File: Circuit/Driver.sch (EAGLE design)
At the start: 1 part

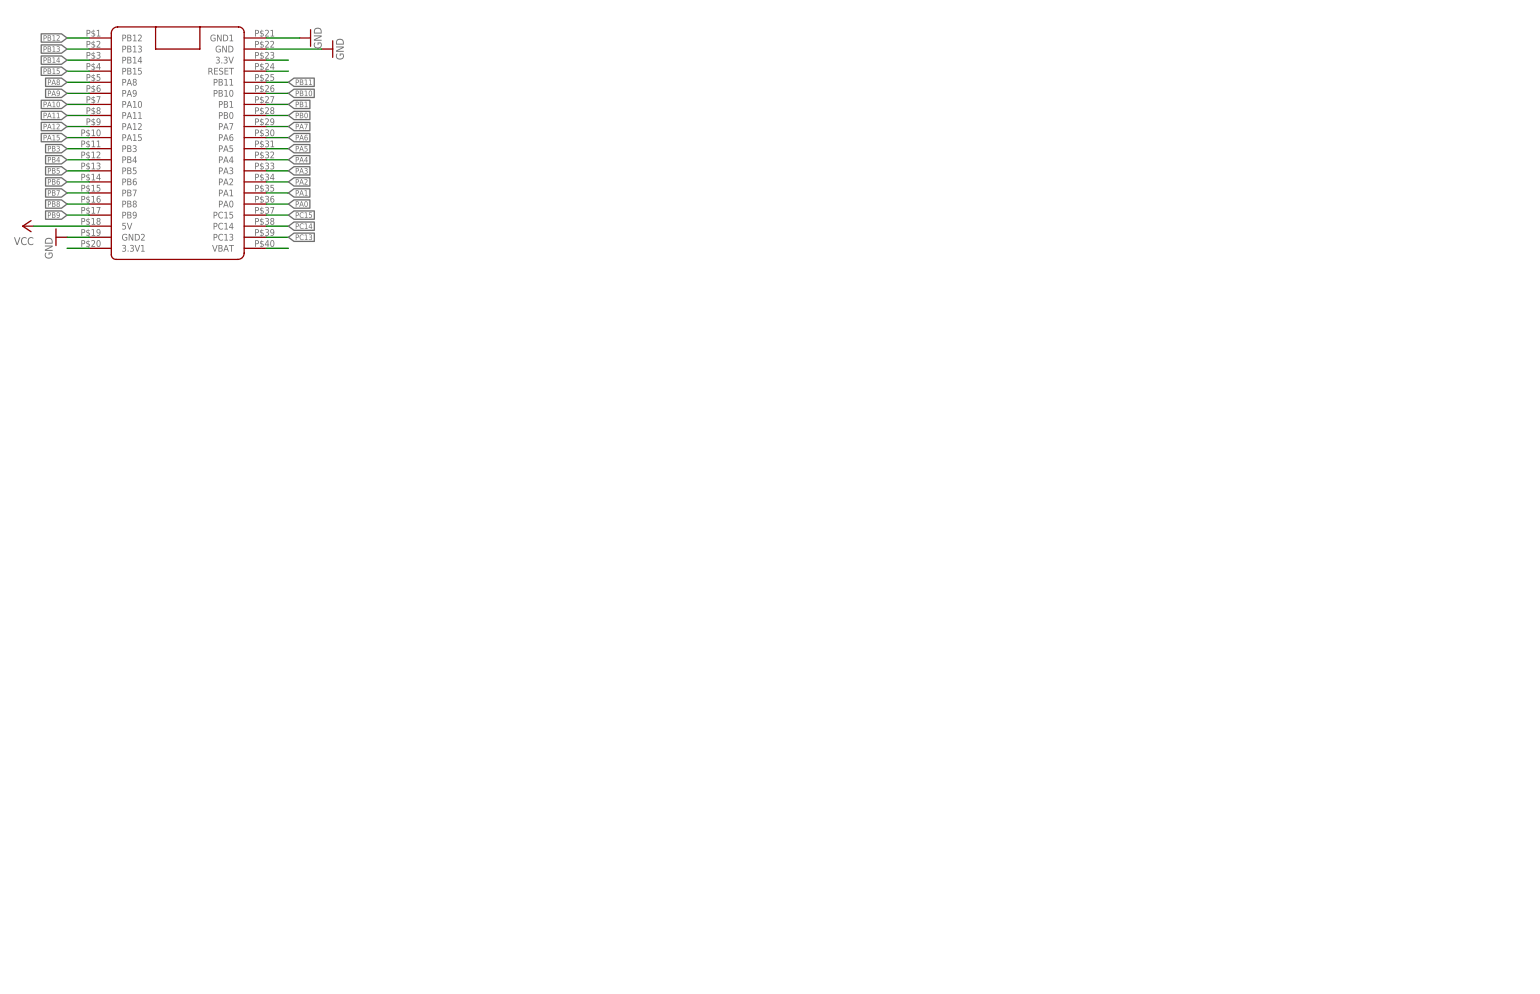
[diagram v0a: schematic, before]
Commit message: Add the mosfets and their driver to the BLDC Driver sch
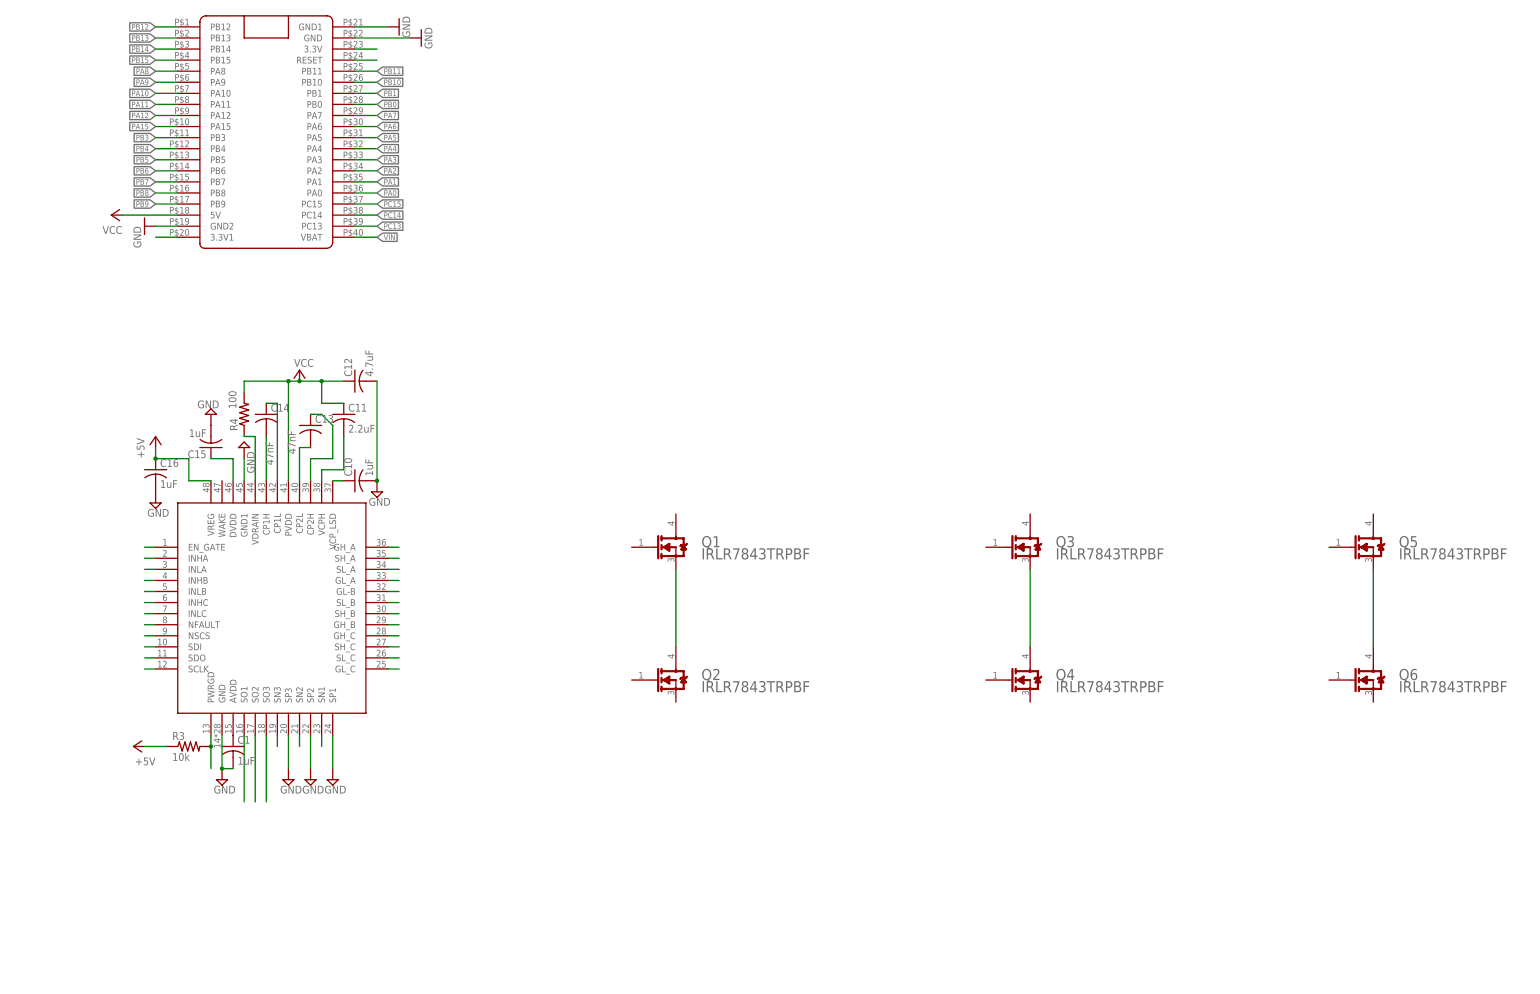
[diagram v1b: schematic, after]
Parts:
- added C1, C10, C15, C16: 1uF, rcl:C-USC0603
- added C11: 2.2uF, rcl:C-USC0603
- added C12: 4.7uF, rcl:C-USC0603
- added C13, C14: 47nF, rcl:C-USC0603
- added Q1, Q2, Q3, Q4, Q5, Q6: INFINEON_IRLR7843TRPBFINFINEON_IRLR7843TRPBF_0_0, IRLR7843:INFINEON_IRLR7843TRPBFINFINEON_IRLR7843TRPBF_0_0
- added R3: 10k, rcl:R-US_R0603
- added R4: 100, rcl:R-US_R0603
- added U$3: DRV8305, BLDC project:DRV8305
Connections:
- net N$20 renamed VIN
- new net +5V: C16.1, R3.1, U$3.VREG
- new net A3: U$3.SO1
- new net A4: U$3.SO2
- new net A5: U$3.SO3
- new net D1: U$3.EN_GATE
- new net D14: U$3.INHB
- new net D15: U$3.INHC
- new net D16: R3.2, U$3.PWRGD
- new net D17: U$3.NSCS
- new net D18: U$3.SDI
- new net D19: U$3.SDO
- new net D20: U$3.SCLK
- new net D8: U$3.INHA
- new net D9: U$3.NFAULT
- new net GH_A1: U$3.GH_A
- new net GH_B1: U$3.GH_B
- new net GH_C1: U$3.GH_C
- new net GL_A1: U$3.GL_A
- new net GL_B1: U$3.GL-B
- new net GL_C1: U$3.GL_C
- new net N$1: Q1.SOURCE, Q2.DRAIN
- new net N$15: C1.1, U$3.AVDD
- new net N$16: C10.1, U$3.VCP_LSD
- new net N$17: C11.2, U$3.VCPH
- new net N$18: C13.2, U$3.CP2L
- new net N$19: C13.1, U$3.CP2H
- new net N$2: Q3.SOURCE, Q4.DRAIN
- new net N$21: C14.2, U$3.CP1H
- new net N$22: C14.1, U$3.CP1L
- new net N$23: R4.1, U$3.VDRAIN
- new net N$24: C15.1, U$3.DVDD
- new net N$25: U$3.INLA
- new net N$26: U$3.INLB
- new net N$27: U$3.INLC
- new net N$5: Q5.SOURCE, Q6.DRAIN
- new net SH_A1: U$3.SH_A
- new net SH_B1: U$3.SH_B
- new net SH_C1: U$3.SH_C
- new net SL_A1: U$3.SL_A, U$3.SN1
- new net SL_B1: U$3.SL_B, U$3.SN2
- new net SL_C1: U$3.SL_C, U$3.SN3
- net GND: now also C1.2, C10.2, C12.2, C15.2, C16.2, U$3.GND, U$3.GND1, U$3.SP1, U$3.SP2, U$3.SP3
- net VCC: now also C11.1, C12.1, R4.2, U$3.PVDD

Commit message: Finish drawing the PCB for 1 stage(not add external layer yet, not autoroutering yet)
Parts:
- removed Q1, Q2, Q3, Q4, Q5, Q6: INFINEON_IRLR7843TRPBFINFINEON_IRLR7843TRPBF_0_0, IRLR7843:INFINEON_IRLR7843TRPBFINFINEON_IRLR7843TRPBF_0_0
- added A, B, C, TP1, TP2: PTR1PAD1-20Y, testpad:PTR1PAD1-20Y
- added C2, C3, C4: 1nF, SparkFun-Capacitors:1.0NF/1000PF-0603-50V-10%
- added C5, C6, C7: 1.0uF, SparkFun-Capacitors:1.0UF-0603-16V-10%-X7R
- added R1, R2, R5: (no value), rcl:R-EU_R2512
- added R6: 10k, SparkFun-Resistors:10KOHM-0603-1/10W-1%
- added U$2, U$4, U$5, U$6, U$7, U$8: IRLR7843, BLDC project:IRLR7843
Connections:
- net D16 renamed PWRGD
- net N$16 renamed VCP_LSD
- net N$17 renamed VCPH
- net N$18 renamed CP2L
- net N$19 renamed CP2H
- net N$21 renamed CP1H
- net N$22 renamed CP1L
- net N$23 renamed VDRAIN
- net N$24 renamed DVDD
- removed net +5V: C16.1, R3.1, U$3.VREG
- removed net A3: U$3.SO1
- removed net A4: U$3.SO2
- removed net A5: U$3.SO3
- removed net D1: U$3.EN_GATE
- removed net D14: U$3.INHB
- removed net D15: U$3.INHC
- removed net D17: U$3.NSCS
- removed net D18: U$3.SDI
- removed net D19: U$3.SDO
- removed net D20: U$3.SCLK
- removed net D8: U$3.INHA
- removed net D9: U$3.NFAULT
- removed net GH_A1: U$3.GH_A
- removed net GH_B1: U$3.GH_B
- removed net GH_C1: U$3.GH_C
- removed net GL_A1: U$3.GL_A
- removed net GL_B1: U$3.GL-B
- removed net GL_C1: U$3.GL_C
- removed net N$1: Q1.SOURCE, Q2.DRAIN
- removed net N$2: Q3.SOURCE, Q4.DRAIN
- removed net N$25: U$3.INLA
- removed net N$26: U$3.INLB
- removed net N$27: U$3.INLC
- removed net N$5: Q5.SOURCE, Q6.DRAIN
- removed net SH_A1: U$3.SH_A
- removed net SH_B1: U$3.SH_B
- removed net SH_C1: U$3.SH_C
- removed net SL_A1: U$3.SL_A, U$3.SN1
- removed net SL_B1: U$3.SL_B, U$3.SN2
- removed net SL_C1: U$3.SL_C, U$3.SN3
- new net GH_A: U$2.G, U$3.GH_A
- new net GH_B: U$3.GH_B, U$5.G
- new net GH_C: U$3.GH_C, U$7.G
- new net GL_A: U$3.GL_A, U$4.G
- new net GL_B: U$3.GL-B, U$6.G
- new net GL_C: U$3.GL_C, U$8.G
- new net PVDD: C11.1, C12.1, U$3.PVDD
- new net SH_A: A.TP, U$2.S, U$3.SH_A, U$4.D
- new net SH_B: B.TP, U$3.SH_B, U$5.S, U$6.D
- new net SH_C: C.TP, U$3.SH_C, U$7.S, U$8.D
- new net SN1: C2.2, R1.2, U$3.SL_A, U$3.SN1, U$4.S
- new net SN2: C3.2, R2.2, U$3.SL_B, U$3.SN2, U$6.S
- new net SN3: C4.2, R5.2, U$3.SL_C, U$3.SN3, U$8.S
- new net VIN1: C6.1
- new net VIN2: C7.1
- new net VREG: C16.1, U$3.VREG
- net GND: now also C2.1, C3.1, C4.1, C5.2, C6.2, C7.2, R1.1, R2.1, R5.1, TP2.TP
- net PA10: now also U$3.INHB
- net PA3: now also U$3.SO3
- net PA4: now also U$3.NSCS
- net PA5: now also U$3.SCLK
- net PA6: now also U$3.SDO
- net PA7: now also U$3.SDI
- net PA8: now also U$3.INHA
- net PA9: now also U$3.INLA
- net PB0: now also U$3.SO2
- net PB1: now also U$3.SO1
- net PB12: now also U$3.EN_GATE
- net PB13: now also R6.2, U$3.NFAULT
- net PB6: now also U$3.INLB
- net PB7: now also U$3.INHC
- net PB8: now also U$3.INLC
- net VCC: now also R3.1, R6.1; no longer C11.1, C12.1, R4.2, U$3.PVDD
- net VIN: now also C5.1, R4.2, TP1.TP, U$2.D, U$5.D, U$7.D
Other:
- note added: "PWM"
